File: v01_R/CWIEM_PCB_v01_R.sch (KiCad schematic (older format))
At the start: 10 parts, among them SW1 SW_PUSH, SW2 SW_PUSH, U1 BC127

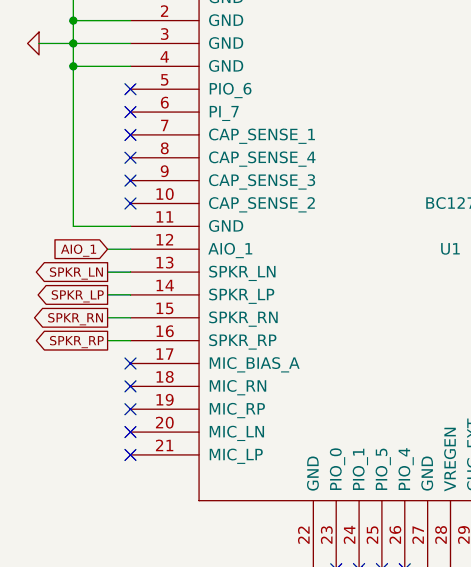
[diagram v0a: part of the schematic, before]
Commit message: Update removes the left channel of the audio circuit.
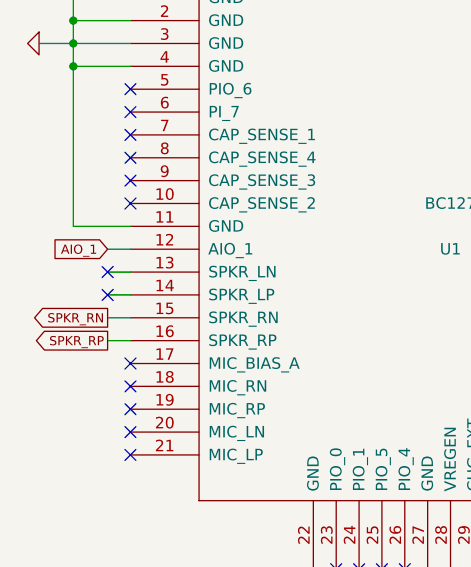
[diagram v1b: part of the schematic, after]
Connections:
- net labels removed: SPKR_LN, SPKR_LP
- no-connect marks 25 -> 27
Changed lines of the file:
@@
 Sheet 1 4
 Title "BC127 circuit"
-Date "7 dec 2014"
+Date "16 jan 2015"
 Rev "0"
 Comp ""
@@
 F1 "audio_circuit.sch" 50
 $EndSheet
-Text GLabel 4000 3600 0    40   Output ~ 0
-SPKR_LN
-Text GLabel 4000 3700 0    40   Output ~ 0
-SPKR_LP
 Text GLabel 4000 3800 0    40   Output ~ 0
 SPKR_RN
@@
 	3850 3400 4100 3400
 Connection ~ 3850 2700
+NoConn ~ 4000 3600
+NoConn ~ 4000 3700
 $EndSCHEMATC

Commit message: Updating entire schematic and footprint selections. Adding jst-ph footprints.
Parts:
- removed D1: LED, ~, symbol LED
- removed R1: 10k, ~, symbol R
- removed R2: 240, ~, symbol R
- removed SW1, SW2: SW_PUSH, ~, symbol SW_PUSH
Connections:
- wire segments 43 -> 34
- no-connect marks 27 -> 29
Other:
- note added: "Currently at 4 LEDs (only LED 1 for final design) and a DIP switch. \n"
- note added: "LED 2 is reserved for Bluetooth Smart use; not useful."
- note removed: "Currently at 5 LEDs, 2 pushbuttons, and a DIP switch. \nNot sure if all will fit on PCB."
- note removed: "There is a mini push button but \nit looks weird in schematic."
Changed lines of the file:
@@
 Sheet 1 4
 Title "BC127 circuit"
-Date "16 jan 2015"
+Date "17 jan 2015"
 Rev "0"
 Comp ""
@@
 NoConn ~ 6900 3300
 NoConn ~ 6900 3400
-$Comp
-L R R1
-U 1 1 5439DCCE
-P 7100 3200
-F 0 "R1" V 7180 3200 40  0000 C CNN
-F 1 "10k" V 7107 3201 40  0000 C CNN
-F 2 "~" V 7030 3200 30  0000 C CNN
-F 3 "~" H 7100 3200 30  0000 C CNN
-	1    7100 3200
-	1    0    0    -1
-$EndComp
-Text GLabel 7250 2950 2    40   Input ~ 0
+Text GLabel 7150 3500 2    40   Input ~ 0
 3.3V
 NoConn ~ 4100 2900
@@
 	6000 4900 6000 5000
 Wire Wire Line
-	7100 3450 7100 3500
-Connection ~ 7100 3500
-Wire Wire Line
-	7250 2950 7100 2950
+	6900 3500 7150 3500
 Text GLabel 4000 3500 0    40   Input ~ 0
 AIO_1
@@
 Text GLabel 8800 4150 2    40   Input ~ 0
 3.3V
-$Comp
-L R R2
-U 1 1 5439FB11
-P 8300 4000
-F 0 "R2" V 8380 4000 40  0000 C CNN
-F 1 "240" V 8307 4001 40  0000 C CNN
-F 2 "~" V 8230 4000 30  0000 C CNN
-F 3 "~" H 8300 4000 30  0000 C CNN
-	1    8300 4000
-	0    -1   -1   0
-$EndComp
 $Comp
 L R R3
@@
 $EndComp
 Wire Wire Line
-	6900 4000 7550 4000
-Wire Wire Line
 	7200 4150 7550 4150
 Wire Wire Line
@@
 	8550 4150 8800 4150
 Wire Wire Line
-	8550 4000 8650 4000
-Wire Wire Line
-	8650 4000 8650 4300
+	8650 4150 8650 4300
 Connection ~ 8650 4150
 Wire Wire Line
 	8650 4300 8550 4300
-Wire Wire Line
-	6900 3500 7500 3500
-$Comp
-L SW_PUSH SW2
-U 1 1 5439FEDB
-P 7800 3500
-F 0 "SW2" H 7950 3610 50  0000 C CNN
-F 1 "SW_PUSH" H 7800 3420 50  0000 C CNN
-F 2 "~" H 7800 3500 60  0000 C CNN
-F 3 "~" H 7800 3500 60  0000 C CNN
-	1    7800 3500
-	1    0    0    -1
-$EndComp
-$Comp
-L GND #PWR03
-U 1 1 5439FF2A
-P 8200 3600
-F 0 "#PWR03" H 8200 3600 30  0001 C CNN
-F 1 "GND" H 8200 3530 30  0001 C CNN
-F 2 "" H 8200 3600 60  0000 C CNN
-F 3 "" H 8200 3600 60  0000 C CNN
-	1    8200 3600
-	1    0    0    -1
-$EndComp
-Wire Wire Line
-	8200 3600 8200 3500
-Wire Wire Line
-	8200 3500 8100 3500
-$Comp
-L SW_PUSH SW1
-U 1 1 5439FFA3
-P 5500 5650
-F 0 "SW1" H 5650 5760 50  0000 C CNN
-F 1 "SW_PUSH" H 5500 5570 50  0000 C CNN
-F 2 "~" H 5500 5650 60  0000 C CNN
-F 3 "~" H 5500 5650 60  0000 C CNN
-	1    5500 5650
-	0    -1   -1   0
-$EndComp
-Wire Wire Line
-	5500 5350 5500 4900
-Text GLabel 5500 6100 3    40   Input ~ 0
-3.3V
-Wire Wire Line
-	5500 5950 5500 6100
 $Comp
 L LED D2
@@
 $EndComp
 $Comp
-L LED D1
-U 1 1 543A0079
-P 7750 4000
-F 0 "D1" H 7750 3900 50  0000 C CNN
-F 1 "LED" H 8000 3950 50  0000 C CNN
-F 2 "~" H 7750 4000 60  0000 C CNN
-F 3 "~" H 7750 4000 60  0000 C CNN
-	1    7750 4000
-	-1   0    0    1
-$EndComp
-$Comp
 L LED D3
 U 1 1 543A007F
@@
 $EndComp
 Wire Wire Line
-	8050 4000 7950 4000
-Wire Wire Line
 	8050 4150 7950 4150
 Wire Wire Line
 	8050 4300 7950 4300
 Text Notes 7100 4550 0    60   ~ 0
-Currently at 5 LEDs, 2 pushbuttons, and a DIP switch. \nNot sure if all will fit on PCB.
-Text Notes 5750 5650 0    60   ~ 0
-There is a mini push button but \nit looks weird in schematic.
-$Comp
-L GND #PWR04
+Currently at 4 LEDs (only LED 1 for final design) and a DIP switch. \n
+$Comp
+L GND #PWR03
 U 1 1 544AFEB2
 P 3700 2600
-F 0 "#PWR04" H 3700 2600 30  0001 C CNN
+F 0 "#PWR03" H 3700 2600 30  0001 C CNN
 F 1 "GND" H 3700 2530 30  0001 C CNN
 F 2 "" H 3700 2600 60  0000 C CNN
@@
 $EndComp
 Wire Wire Line
-	4100 2600 3700 2600
+	3700 2600 4100 2600
 Text Notes 6450 5100 0    60   ~ 0
 I had to make CHG_EXT an output pin \n(base of PNP transistor is an input pin).
@@
 NoConn ~ 4000 3600
 NoConn ~ 4000 3700
+NoConn ~ 5500 4900
+NoConn ~ 6900 4000
+Text Notes 7550 4000 0    60   ~ 0
+LED 2 is reserved for Bluetooth Smart use; not useful.
 $EndSCHEMATC

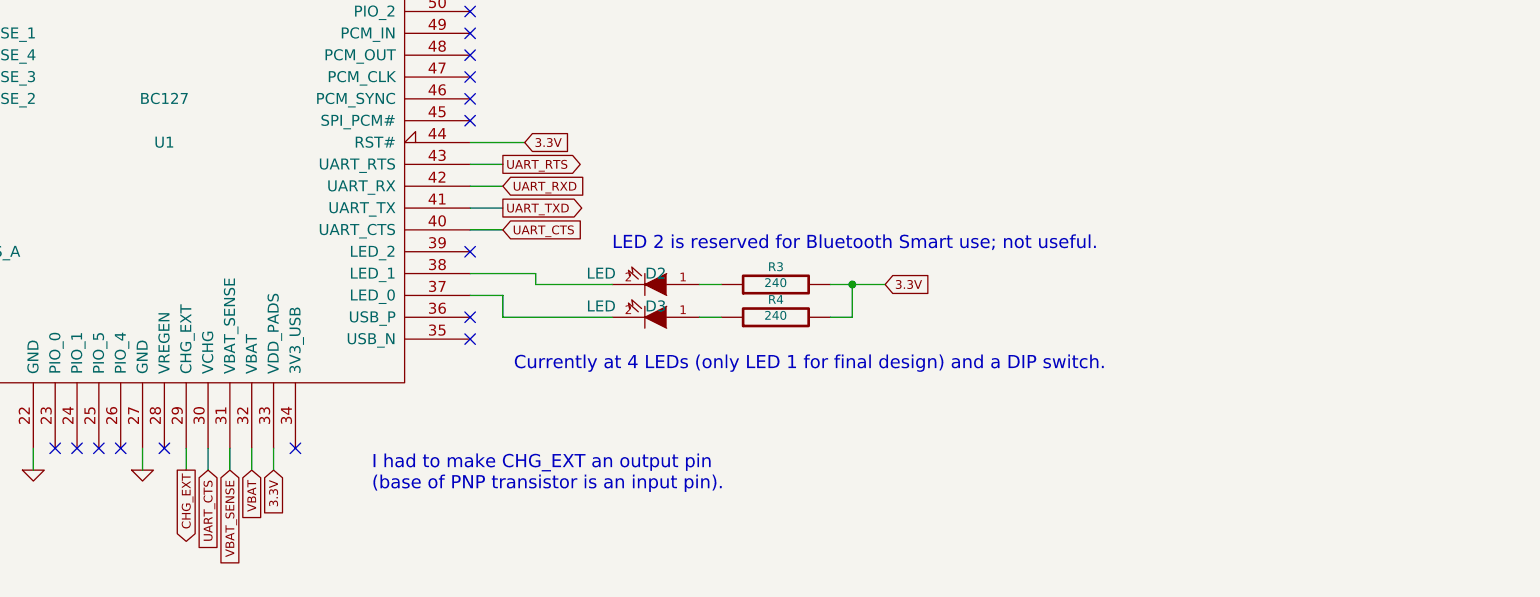
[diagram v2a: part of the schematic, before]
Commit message: Adding very rough initial version of PCB. The BA driver pads were not exact yet (based off of a Sonion driver datasheet).
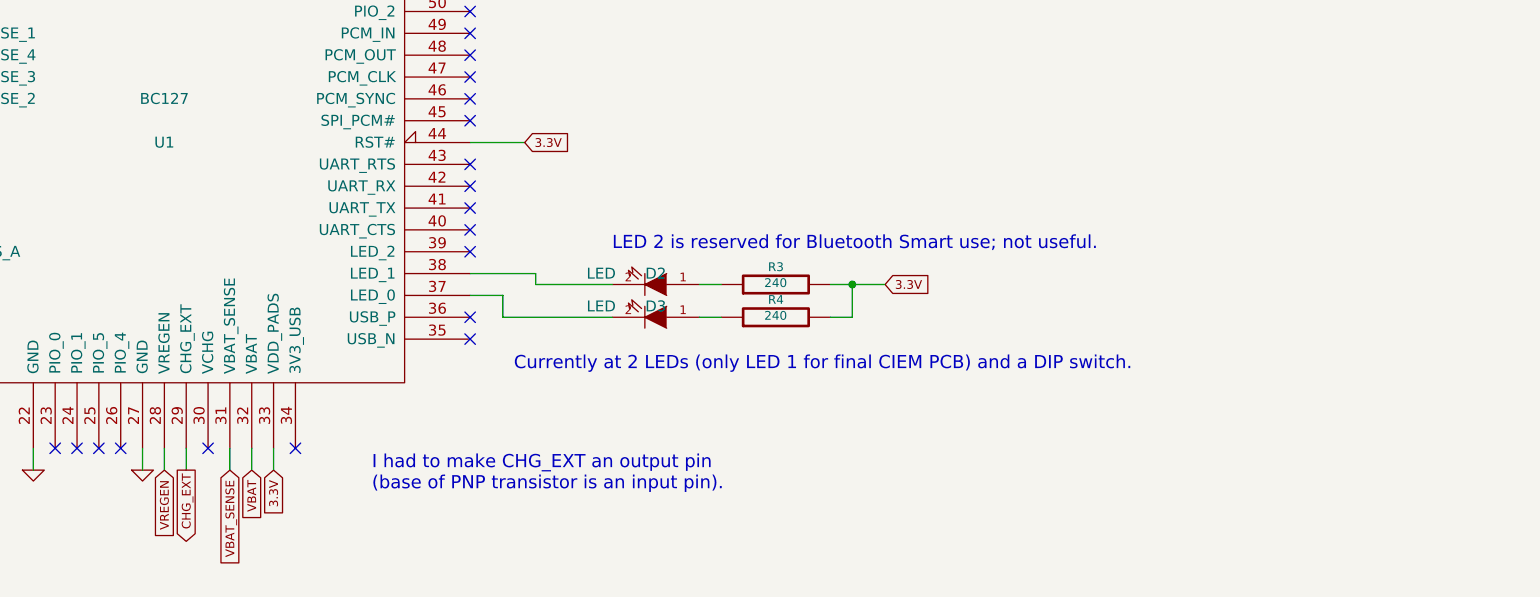
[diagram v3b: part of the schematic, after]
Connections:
- net VREGEN: now reaches U1.28 (VREGEN)
- net UART_CTS: no longer names the net of U1.30 (VCHG)
- net UART_CTS: no longer U1.40 (UART_CTS)
- net UART_RTS: no longer names the net of U1.43 (UART_RTS)
- net UART_RXD: no longer names the net of U1.42 (UART_RX)
- net UART_TXD: no longer names the net of U1.41 (UART_TX)
- no-connect marks 29 -> 33
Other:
- note added: "Currently at 2 LEDs (only LED 1 for final CIEM PCB) and a DIP switch. \n"
- note removed: "Currently at 4 LEDs (only LED 1 for final design) and a DIP switch. \n"
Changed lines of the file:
@@
 Sheet 1 4
 Title "BC127 circuit"
-Date "17 jan 2015"
+Date "18 jan 2015"
 Rev "0"
 Comp ""
@@
 F1 "comm_circuit.sch" 50
 $EndSheet
-Text GLabel 7050 3700 2    40   Input ~ 0
-UART_RXD
-Text GLabel 7050 3900 2    40   Input ~ 0
-UART_CTS
-Text GLabel 7050 3800 2    40   Output ~ 0
-UART_TXD
-Text GLabel 7050 3600 2    40   Output ~ 0
-UART_RTS
 $Sheet
 S 11900 3400 1650 1400
@@
 	1    0    0    -1
 $EndComp
-Text GLabel 5700 5000 3    40   Input ~ 0
-UART_CTS
 Text GLabel 5800 5000 3    40   Input ~ 0
 VBAT_SENSE
@@
 	4100 3900 4000 3900
 Wire Wire Line
-	7050 3700 6900 3700
-Wire Wire Line
-	7050 3600 6900 3600
-Wire Wire Line
-	7050 3800 6900 3800
-Wire Wire Line
-	7050 3900 6900 3900
-Wire Wire Line
 	5400 4900 5400 5000
 Wire Wire Line
 	4900 4900 4900 5000
-Wire Wire Line
-	5700 5000 5700 4900
 Wire Wire Line
 	5800 5000 5800 4900
@@
 	8050 4300 7950 4300
 Text Notes 7100 4550 0    60   ~ 0
-Currently at 4 LEDs (only LED 1 for final design) and a DIP switch. \n
+Currently at 2 LEDs (only LED 1 for final CIEM PCB) and a DIP switch. \n
 $Comp
 L GND #PWR03
@@
 NoConn ~ 4000 3600
 NoConn ~ 4000 3700
-NoConn ~ 5500 4900
 NoConn ~ 6900 4000
 Text Notes 7550 4000 0    60   ~ 0
 LED 2 is reserved for Bluetooth Smart use; not useful.
+NoConn ~ 6900 3600
+NoConn ~ 6900 3700
+NoConn ~ 6900 3800
+NoConn ~ 6900 3900
+NoConn ~ 5700 4900
+Text GLabel 5500 5000 3    40   Input ~ 0
+VREGEN
+Wire Wire Line
+	5500 5000 5500 4900
 $EndSCHEMATC
